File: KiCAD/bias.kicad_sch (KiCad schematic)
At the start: 52 parts, among them Q2 2N7000, Q3 2N7000, U10 OPA454, U11 LM4040LP-5, U12 LM393, U13 OPA1641, U14 OPA1641, U5 OPA454, U9 LM7805_TO220

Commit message: schematic: I2C topology flip + CD14538B heartbeat + pre-layout audit
- Documentation updates for the STEMMA-QT topology flip (MCP4728 upstream
  of Si5351): design_review_7-5-26 C1 marked resolved, build_checklist
  Phase 1 gets the 6-step first-boot procedure, cw_envelope_keyer I2C
  address section rewritten, front_panel_interface signal-chain diagram
  refreshed.
- CD14538B dual retriggerable monostable added to xmitter.kicad_sym
  (PDIP-16, pinout verified against datasheet fig. 1), plus datasheet
  file.
- Arduino sheet: CD14538B heartbeat topology on Q5 HV contactor -- U18
  + R30 470K + C41 1uF timing (t_w ~470 ms), Q7 series FET stack,
  C42/C43 VDD bypass and bulk.
- Pre-layout audit output as Documentation/punch_list_7-6-26.txt (list
  of blockers before PCB layout, ordered by severity).

Co-Authored-By: Claude Opus 4.7 (1M context) <noreply@anthropic.com>
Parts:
- added J11: GRID_BIAS, symbol Connector:Conn_01x02_Pin
- added J12: CATHODE_SENSE, symbol Connector:Conn_01x02_Pin
- added J14: Conn_01x02_Pin, symbol Connector:Conn_01x02_Pin
- added TP10: CRASH_A, Connector_PinHeader_2.54mm:PinHeader_1x01_P2.54mm_Vertical, symbol xmitter:xTP
- added TP8: GRID_CRASH, Connector_PinHeader_2.54mm:PinHeader_1x01_P2.54mm_Vertical, symbol xmitter:xTP
- added TP9: CRASH_B, Connector_PinHeader_2.54mm:PinHeader_1x01_P2.54mm_Vertical, symbol xmitter:xTP
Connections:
- net CATHODE_SENSE_A: now also J12.1 (Pin_1)
- net CATHODE_SENSE_B: now also J12.2 (Pin_2)
- net GND: now also J14.2 (Pin_2)
- net GRID_BIAS_A_OUT: now also J11.2 (Pin_2)
- net GRID_BIAS_B_OUT: now also J11.1 (Pin_1)
- net GRID_BLOCK_CRASH: now also J14.1 (Pin_1), TP8.1
- net I_CATHODE_A: now also TP10.1
- net I_CATHODE_B: now also TP9.1

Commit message: kicad: convert hierarchical labels to globals (Path A) + unify _OUT/_IN pairs
- 58 hierarchical_label -> global_label conversions across the six active
  sheets. Standard KiCad 10 global_label form with fields_autoplaced +
  Intersheetrefs property.
- Stripped 36 vestigial sheet pins, 28 stitching wires, 2 junctions, 4
  labels from the root sheet. Sheet blocks remain; each is now a pure
  container with globals doing the cross-sheet connectivity by name.
- Renamed three OUT/IN pairs to unified names so same-name globals
  auto-connect:
    GRID_CTL_A_OUT + GRID_CTL_A_IN -> GRID_CTL_A
    GRID_CTL_B_OUT + GRID_CTL_B_IN -> GRID_CTL_B
    RAW_RF_OUT     + RAW_RF_IN     -> RAW_RF
- tools/convert_hier_to_global.py and tools/strip_root_stitching.py:
  reusable if we ever need to redo this.
- Documentation/punch_list_7-6-26.txt: mark B1a-e, L1, L2 resolved; add
  M6 (cosmetic) about GRID_CTL_A's label-at-pin-origin idiom; correct
  the earlier GRID_CTL_A false positive with the verified chain
  MCP4728 U8 VC -> R_PADA -> OPA454 U5 IN+ + Q3 drain.

Co-Authored-By: Claude Opus 4.7 (1M context) <noreply@anthropic.com>
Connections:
- net GRID_CTL_A_IN renamed GRID_CTL_A
- net GRID_CTL_B_IN renamed GRID_CTL_B
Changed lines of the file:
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@@
 		)
 	)
-	(hierarchical_label "+5V_REF"
+	(global_label "+5V_REF"
 		(shape output)
 		(at 22.86 118.11 180)
-		(effects
-			(font
-				(size 1.27 1.27)
-			)
-			(justify right)
-		)
-	)
-	(hierarchical_label "GRID_CTL_B_IN"
+		(fields_autoplaced yes)
+		(effects
+			(font
+				(size 1.27 1.27)
+			)
+			(justify right)
+		)
+		(property "Intersheetrefs" "${INTERSHEET_REFS}"
+			(at 22.86 118.11 0)
+			(effects
+				(font
+					(size 1.27 1.27)
+				)
+				(hide yes)
+			)
+		)
+	)
+	(global_label "GRID_CTL_B"
 		(shape input)
 		(at 58.42 125.73 180)
-		(effects
-			(font
-				(size 1.27 1.27)
-			)
-			(justify right)
-		)
-	)
-	(hierarchical_label "GRID_CTL_A_IN"
+		(fields_autoplaced yes)
+		(effects
+			(font
+				(size 1.27 1.27)
+			)
+			(justify right)
+		)
+		(property "Intersheetrefs" "${INTERSHEET_REFS}"
+			(at 58.42 125.73 0)
+			(effects
+				(font
+					(size 1.27 1.27)
+				)
+				(hide yes)
+			)
+		)
+	)
+	(global_label "GRID_CTL_A"
 		(shape input)
 		(at 69.85 86.36 180)
-		(effects
-			(font
-				(size 1.27 1.27)
-			)
-			(justify right)
-		)
-	)
-	(hierarchical_label "I_CATHODE_B"
+		(fields_autoplaced yes)
+		(effects
+			(font
+				(size 1.27 1.27)
+			)
+			(justify right)
+		)
+		(property "Intersheetrefs" "${INTERSHEET_REFS}"
+			(at 69.85 86.36 0)
+			(effects
+				(font
+					(size 1.27 1.27)
+				)
+				(hide yes)
+			)
+		)
+	)
+	(global_label "I_CATHODE_B"
 		(shape output)
 		(at 223.52 81.28 0)
-		(effects
-			(font
-				(size 1.27 1.27)
-			)
-			(justify left)
-		)
-	)
-	(hierarchical_label "+5V_REF"
+		(fields_autoplaced yes)
+		(effects
+			(font
+				(size 1.27 1.27)
+			)
+			(justify left)
+		)
+		(property "Intersheetrefs" "${INTERSHEET_REFS}"
+			(at 223.52 81.28 0)
+			(effects
+				(font
+					(size 1.27 1.27)
+				)
+				(hide yes)
+			)
+		)
+	)
+	(global_label "+5V_REF"
 		(shape output)
 		(at 162.56 87.63 90)
-		(effects
-			(font
-				(size 1.27 1.27)
-			)
-			(justify left)
-		)
-	)
-	(hierarchical_label "GRID_BIAS_A_OUT"
+		(fields_autoplaced yes)
+		(effects
+			(font
+				(size 1.27 1.27)
+			)
+			(justify left)
+		)
+		(property "Intersheetrefs" "${INTERSHEET_REFS}"
+			(at 162.56 87.63 0)
+			(effects
+				(font
+					(size 1.27 1.27)
+				)
+				(hide yes)
+			)
+		)
+	)
+	(global_label "GRID_BIAS_A_OUT"
 		(shape output)
 		(at 119.38 82.55 0)
-		(effects
-			(font
-				(size 1.27 1.27)
-			)
-			(justify left)
-		)
-	)
-	(hierarchical_label "CATHODE_SENSE_B"
+		(fields_autoplaced yes)
+		(effects
+			(font
+				(size 1.27 1.27)
+			)
+			(justify left)
+		)
+		(property "Intersheetrefs" "${INTERSHEET_REFS}"
+			(at 119.38 82.55 0)
+			(effects
+				(font
+					(size 1.27 1.27)
+				)
+				(hide yes)
+			)
+		)
+	)
+	(global_label "CATHODE_SENSE_B"
 		(shape input)
 		(at 186.69 81.28 270)
-		(effects
-			(font
-				(size 1.27 1.27)
-			)
-			(justify right)
-		)
-	)
-	(hierarchical_label "GRID_BLOCK_CRASH"
+		(fields_autoplaced yes)
+		(effects
+			(font
+				(size 1.27 1.27)
+			)
+			(justify right)
+		)
+		(property "Intersheetrefs" "${INTERSHEET_REFS}"
+			(at 186.69 81.28 0)
+			(effects
+				(font
+					(size 1.27 1.27)
+				)
+				(hide yes)
+			)
+		)
+	)
+	(global_label "GRID_BLOCK_CRASH"
 		(shape output)
 		(at 50.8 132.08 180)
-		(effects
-			(font
-				(size 1.27 1.27)
-			)
-			(justify right)
-		)
-	)
-	(hierarchical_label "CATHODE_SENSE_A"
+		(fields_autoplaced yes)
+		(effects
+			(font
+				(size 1.27 1.27)
+			)
+			(justify right)
+		)
+		(property "Intersheetrefs" "${INTERSHEET_REFS}"
+			(at 50.8 132.08 0)
+			(effects
+				(font
+					(size 1.27 1.27)
+				)
+				(hide yes)
+			)
+		)
+	)
+	(global_label "CATHODE_SENSE_A"
 		(shape input)
 		(at 181.61 40.64 180)
-		(effects
-			(font
-				(size 1.27 1.27)
-			)
-			(justify right)
-		)
-	)
-	(hierarchical_label "GRID_BIAS_B_OUT"
+		(fields_autoplaced yes)
+		(effects
+			(font
+				(size 1.27 1.27)
+			)
+			(justify right)
+		)
+		(property "Intersheetrefs" "${INTERSHEET_REFS}"
+			(at 181.61 40.64 0)
+			(effects
+				(font
+					(size 1.27 1.27)
+				)
+				(hide yes)
+			)
+		)
+	)
+	(global_label "GRID_BIAS_B_OUT"
 		(shape output)
 		(at 120.65 121.92 0)
-		(effects
-			(font
-				(size 1.27 1.27)
-			)
-			(justify left)
-		)
-	)
-	(hierarchical_label "I_CATHODE_A"
+		(fields_autoplaced yes)
+		(effects
+			(font
+				(size 1.27 1.27)
+			)
+			(justify left)
+		)
+		(property "Intersheetrefs" "${INTERSHEET_REFS}"
+			(at 120.65 121.92 0)
+			(effects
+				(font
+					(size 1.27 1.27)
+				)
+				(hide yes)
+			)
+		)
+	)
+	(global_label "I_CATHODE_A"
 		(shape output)
 		(at 210.82 43.18 0)
-		(effects
-			(font
-				(size 1.27 1.27)
-			)
-			(justify left)
-		)
-	)
-	(hierarchical_label "GRID_BLOCK_CRASH"
+		(fields_autoplaced yes)
+		(effects
+			(font
+				(size 1.27 1.27)
+			)
+			(justify left)
+		)
+		(property "Intersheetrefs" "${INTERSHEET_REFS}"
+			(at 210.82 43.18 0)
+			(effects
+				(font
+					(size 1.27 1.27)
+				)
+				(hide yes)
+			)
+		)
+	)
+	(global_label "GRID_BLOCK_CRASH"
 		(shape output)
 		(at 262.89 57.15 0)
-		(effects
-			(font
-				(size 1.27 1.27)
-			)
-			(justify left)
-		)
-	)
-	(hierarchical_label "CATHODE_SENSE_B"
+		(fields_autoplaced yes)
+		(effects
+			(font
+				(size 1.27 1.27)
+			)
+			(justify left)
+		)
+		(property "Intersheetrefs" "${INTERSHEET_REFS}"
+			(at 262.89 57.15 0)
+			(effects
+				(font
+					(size 1.27 1.27)
+				)
+				(hide yes)
+			)
+		)
+	)
+	(global_label "CATHODE_SENSE_B"
 		(shape input)
 		(at 152.4 50.8 0)
-		(effects
-			(font
-				(size 1.27 1.27)
-			)
-			(justify left)
-		)
-	)
-	(hierarchical_label "CATHODE_SENSE_A"
+		(fields_autoplaced yes)
+		(effects
+			(font
+				(size 1.27 1.27)
+			)
+			(justify left)
+		)
+		(property "Intersheetrefs" "${INTERSHEET_REFS}"
+			(at 152.4 50.8 0)
+			(effects
+				(font
+					(size 1.27 1.27)
+				)
+				(hide yes)
+			)
+		)
+	)
+	(global_label "CATHODE_SENSE_A"
 		(shape input)
 		(at 152.4 48.26 0)
-		(effects
-			(font
-				(size 1.27 1.27)
-			)
-			(justify left)
-		)
-	)
+		(fields_autoplaced yes)
+		(effects
+			(font
+				(size 1.27 1.27)
+			)
+			(justify left)
+		)
+		(property "Intersheetrefs" "${INTERSHEET_REFS}"
+			(at 152.4 48.26 0)
+			(effects
+				(font
+					(size 1.27 1.27)
+				)
+				(hide yes)
+			)
+		)
+	)

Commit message: kicad: fill 9 remaining footprints across active sheets
- arduino: R30 470K (R_Axial_DIN0207 horizontal), C41 1uF (rect L7.2mm),
  C42 100nF (disc D5mm P5mm), C43 10uF (radial polarized D5mm P2mm)
- bias: J11 (GRID_BIAS), J12 (CATHODE_SENSE), J14 -- all PinHeader_1x02
  vertical THT
- buffer_keyer: J13 -- PinHeader_1x05 vertical THT
- interface: J15 -- PinHeader_1x03 vertical THT

C41/C42/C43 filled by re-running tools/assign_cap_footprints.py which
already had the intended mappings. R30 and the connectors done by hand
via a one-off script.

Only U2 (Metro) remains footprint-less, intentionally off-PCB.

Punch list updates for today's ERC pass + user's schematic edits:
- B3 (footprints) resolved.
- B4d/B4e (TP2/TP7 to MOD_RF+/-) resolved -- user verified junction dots
  + wires in KiCad. TP3 = SCL is intentional (I2C debug probe access).
- M5 (TX_LED) previously resolved -- LED wired in parallel with T/R
  relay coil, no Metro GPIO needed.
- B2 (paddle) rewritten for the actual design: J10 = 2-conductor 1/4"
  phone plug, tip -> Metro D5, sleeve -> GND.

vfo.kicad_sch diff is KiCad's own canonicalization of Intersheetrefs
property (show_name/do_not_autoplace fields shuffled) from opening +
saving; contents equivalent.

Co-Authored-By: Claude Opus 4.7 (1M context) <noreply@anthropic.com>
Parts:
- J11, J12, J14: footprint (none) -> Connector_PinHeader_2.54mm:PinHeader_1x02_P2.54mm_Vertical
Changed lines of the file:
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@@
 		(property "Intersheetrefs" "${INTERSHEET_REFS}"
 			(at 22.86 118.11 0)
+			(hide yes)
+			(show_name no)
+			(do_not_autoplace no)
 			(effects
 				(font
 					(size 1.27 1.27)
 				)
-				(hide yes)
 			)
 		)
@@
 		(property "Intersheetrefs" "${INTERSHEET_REFS}"
 			(at 58.42 125.73 0)
+			(hide yes)
+			(show_name no)
+			(do_not_autoplace no)
 			(effects
 				(font
 					(size 1.27 1.27)
 				)
-				(hide yes)
 			)
 		)
@@
 		(property "Intersheetrefs" "${INTERSHEET_REFS}"
 			(at 69.85 86.36 0)
+			(hide yes)
+			(show_name no)
+			(do_not_autoplace no)
 			(effects
 				(font
 					(size 1.27 1.27)
 				)
-				(hide yes)
 			)
 		)
@@
 		(property "Intersheetrefs" "${INTERSHEET_REFS}"
 			(at 223.52 81.28 0)
+			(hide yes)
+			(show_name no)
+			(do_not_autoplace no)
 			(effects
 				(font
 					(size 1.27 1.27)
 				)
-				(hide yes)
 			)
 		)
@@
 		(property "Intersheetrefs" "${INTERSHEET_REFS}"
 			(at 162.56 87.63 0)
+			(hide yes)
+			(show_name no)
+			(do_not_autoplace no)
 			(effects
 				(font
 					(size 1.27 1.27)
 				)
-				(hide yes)
 			)
 		)
@@
 		(property "Intersheetrefs" "${INTERSHEET_REFS}"
 			(at 119.38 82.55 0)
+			(hide yes)
+			(show_name no)
+			(do_not_autoplace no)
 			(effects
 				(font
 					(size 1.27 1.27)
 				)
-				(hide yes)
 			)
 		)
@@
 		(property "Intersheetrefs" "${INTERSHEET_REFS}"
 			(at 186.69 81.28 0)
+			(hide yes)
+			(show_name no)
+			(do_not_autoplace no)
 			(effects
 				(font
 					(size 1.27 1.27)
 				)
-				(hide yes)
 			)
 		)
@@
 		(property "Intersheetrefs" "${INTERSHEET_REFS}"
 			(at 50.8 132.08 0)
+			(hide yes)
+			(show_name no)
+			(do_not_autoplace no)
 			(effects
 				(font
 					(size 1.27 1.27)
 				)
-				(hide yes)
 			)
 		)
@@
 		(property "Intersheetrefs" "${INTERSHEET_REFS}"
 			(at 181.61 40.64 0)
+			(hide yes)
+			(show_name no)
+			(do_not_autoplace no)
 			(effects
 				(font
 					(size 1.27 1.27)
 				)
-				(hide yes)
 			)
 		)
@@
 		(property "Intersheetrefs" "${INTERSHEET_REFS}"
 			(at 120.65 121.92 0)
+			(hide yes)
+			(show_name no)
+			(do_not_autoplace no)
 			(effects
 				(font
 					(size 1.27 1.27)
 				)
-				(hide yes)
 			)
 		)
@@
 		(property "Intersheetrefs" "${INTERSHEET_REFS}"
 			(at 210.82 43.18 0)
+			(hide yes)
+			(show_name no)
+			(do_not_autoplace no)
 			(effects
 				(font
 					(size 1.27 1.27)
 				)
-				(hide yes)
 			)
 		)
@@
 		(property "Intersheetrefs" "${INTERSHEET_REFS}"
 			(at 262.89 57.15 0)
+			(hide yes)
+			(show_name no)
+			(do_not_autoplace no)
 			(effects
 				(font
 					(size 1.27 1.27)
 				)
-				(hide yes)
 			)
 		)
@@
 		(property "Intersheetrefs" "${INTERSHEET_REFS}"
 			(at 152.4 50.8 0)
+			(hide yes)
+			(show_name no)
+			(do_not_autoplace no)
 			(effects
 				(font
 					(size 1.27 1.27)
 				)
-				(hide yes)
 			)
 		)
@@
 		(property "Intersheetrefs" "${INTERSHEET_REFS}"
 			(at 152.4 48.26 0)
+			(hide yes)
+			(show_name no)
+			(do_not_autoplace no)
 			(effects
 				(font
 					(size 1.27 1.27)
 				)
-				(hide yes)
 			)
 		)
@@
 			)
 		)
-		(property "Footprint" ""
+		(property "Footprint" "Connector_PinHeader_2.54mm:PinHeader_1x02_P2.54mm_Vertical"
 			(at 261.62 48.26 0)
 			(hide yes)
@@
 			)
 		)
-		(property "Footprint" ""
+		(property "Footprint" "Connector_PinHeader_2.54mm:PinHeader_1x02_P2.54mm_Vertical"
 			(at 147.32 48.26 0)
 			(hide yes)
@@
 			)
 		)
-		(property "Footprint" ""
+		(property "Footprint" "Connector_PinHeader_2.54mm:PinHeader_1x02_P2.54mm_Vertical"
 			(at 119.38 104.14 0)
 			(hide yes)

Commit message: kicad: PWR_FLAGs added, most +3.3V converted to 3V3, VFO renames + J2 NC
User work today:
- Placed PWR_FLAGs to silence "power_pin_not_driven" ERC errors for VEE,
  +12V, -90V rails (see B5a-B5f in the punch list)
- Converted 6 of 7 +3.3V power symbols to 3V3 global labels project-wide
  (one +3.3V remains on bias sheet, resolves next pass)
- VFO sheet: C_coup -> C_IN1, R6 -> RD1 (both were unannotated / duplicate
  ref designators; ERC B4a and B4b now resolved)
- buffer_keyer: J2 pin 2 gets a no_connect flag (B4c resolved); TP2 and
  TP7 electrically wired to MOD_RF_OUT+/- via junctions (B4d/e resolved)

Punch list updates:
- B3 (footprints) marked done
- B4a/b/c marked done
- M5 (TX LED) confirmed resolved (external LED across T/R relay coil)
- B2 (paddle) rewritten for the actual 2-conductor 1/4" plug scheme

Current ERC status: 61 errors, 0 warnings (from 74 + 2 originally).
Remaining real bugs: unannotated C_IN + duplicate C_IN1 on buffer_keyer,
misplaced #FLG04 on Metro's 3V3 pin, one leftover +3.3V on bias. Rest
are the known-non-issue plateau.

Co-Authored-By: Claude Opus 4.7 (1M context) <noreply@anthropic.com>
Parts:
- renumbered R_FA to R_FA1, R_FB to R_FB1, R_GA to R_GA1, R_GATE to R_GATE1, R_GB to R_GB1, R_GLA to R_GLA1, R_GLB to R_GLB1, R_PADA to R_PADA1, R_PADB to R_PADB1, R_Z to R_Z1
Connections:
- net +3.3V renamed 3V3

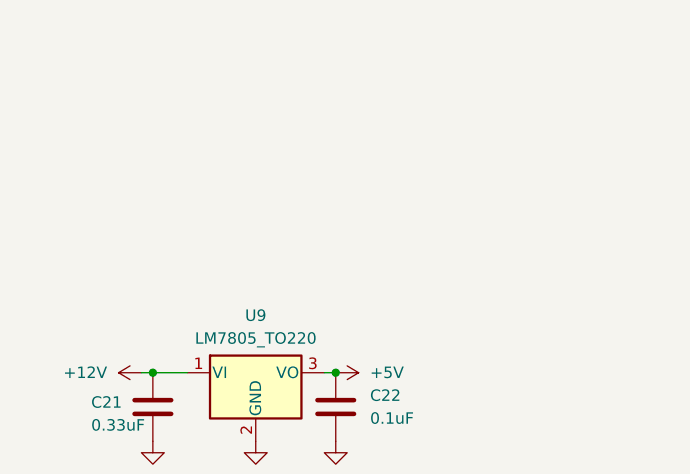
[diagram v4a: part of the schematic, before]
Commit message: kicad: buffer_keyer LM7805 local, J3 to bias, more testpoints
- buffer_keyer.kicad_sch: LM7805 5V regulator + bypass caps copied over
  from bias sheet so this board only needs +12V input. Multiple new
  testpoints added: T1/T2 collectors, LDAC (near U8), DAC output (near
  U4), and one placeholder. Signals now covered end-to-end for
  envelope + modulator debugging.
- bias.kicad_sch: J3 relocated here (was on buffer_keyer). J3 pin 1
  VEE previously conflicted with the new local VEE generator on
  buffer_keyer -- moving J3 to bias also means it belongs on the
  bias board once that becomes its own PCB. VEE pin will be
  repurposed as GND on that side.
- arduino.kicad_sch: incidental annotation edits.

Architectural decision recorded (not yet acted on): bias will become
a separate PCB, both boards in the same top-mount subchassis, ribbon
between them, only the four tube-facing signals (GRID_BIAS_A/B_OUT,
CATHODE_SENSE_A/B) cross into the main chassis via a round bulkhead.
I_CATHODE_A/B and GRID_BLOCK_CRASH will reach the Metro via direct
jumpers from bias-PCB header pins (Path B), not through the ribbon.

Co-Authored-By: Claude Opus 4.7 <noreply@anthropic.com>
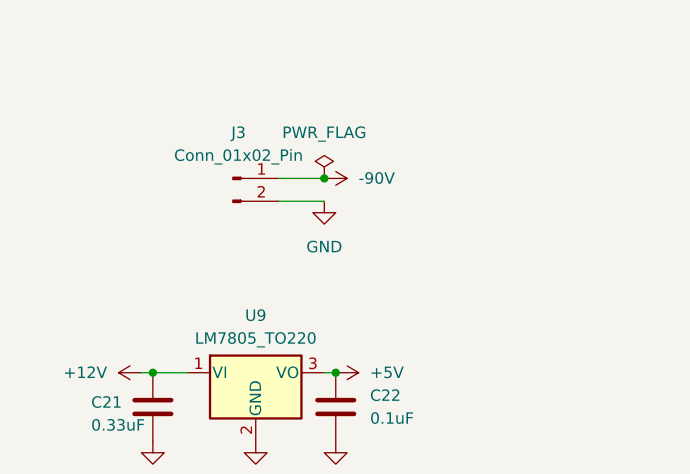
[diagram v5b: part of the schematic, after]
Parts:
- added J3: Conn_01x02_Pin, Connector_PinHeader_2.54mm:PinHeader_1x02_P2.54mm_Vertical, symbol Connector:Conn_01x02_Pin
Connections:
- net -90V: now also J3.1 (Pin_1)
- net GND: now also J3.2 (Pin_2)
